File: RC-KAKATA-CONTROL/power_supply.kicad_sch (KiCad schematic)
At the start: 51 parts, among them J3 Screw_Terminal_01x02, J4 Screw_Terminal_01x02, U1 PS-TO220, U2 PS-TO220

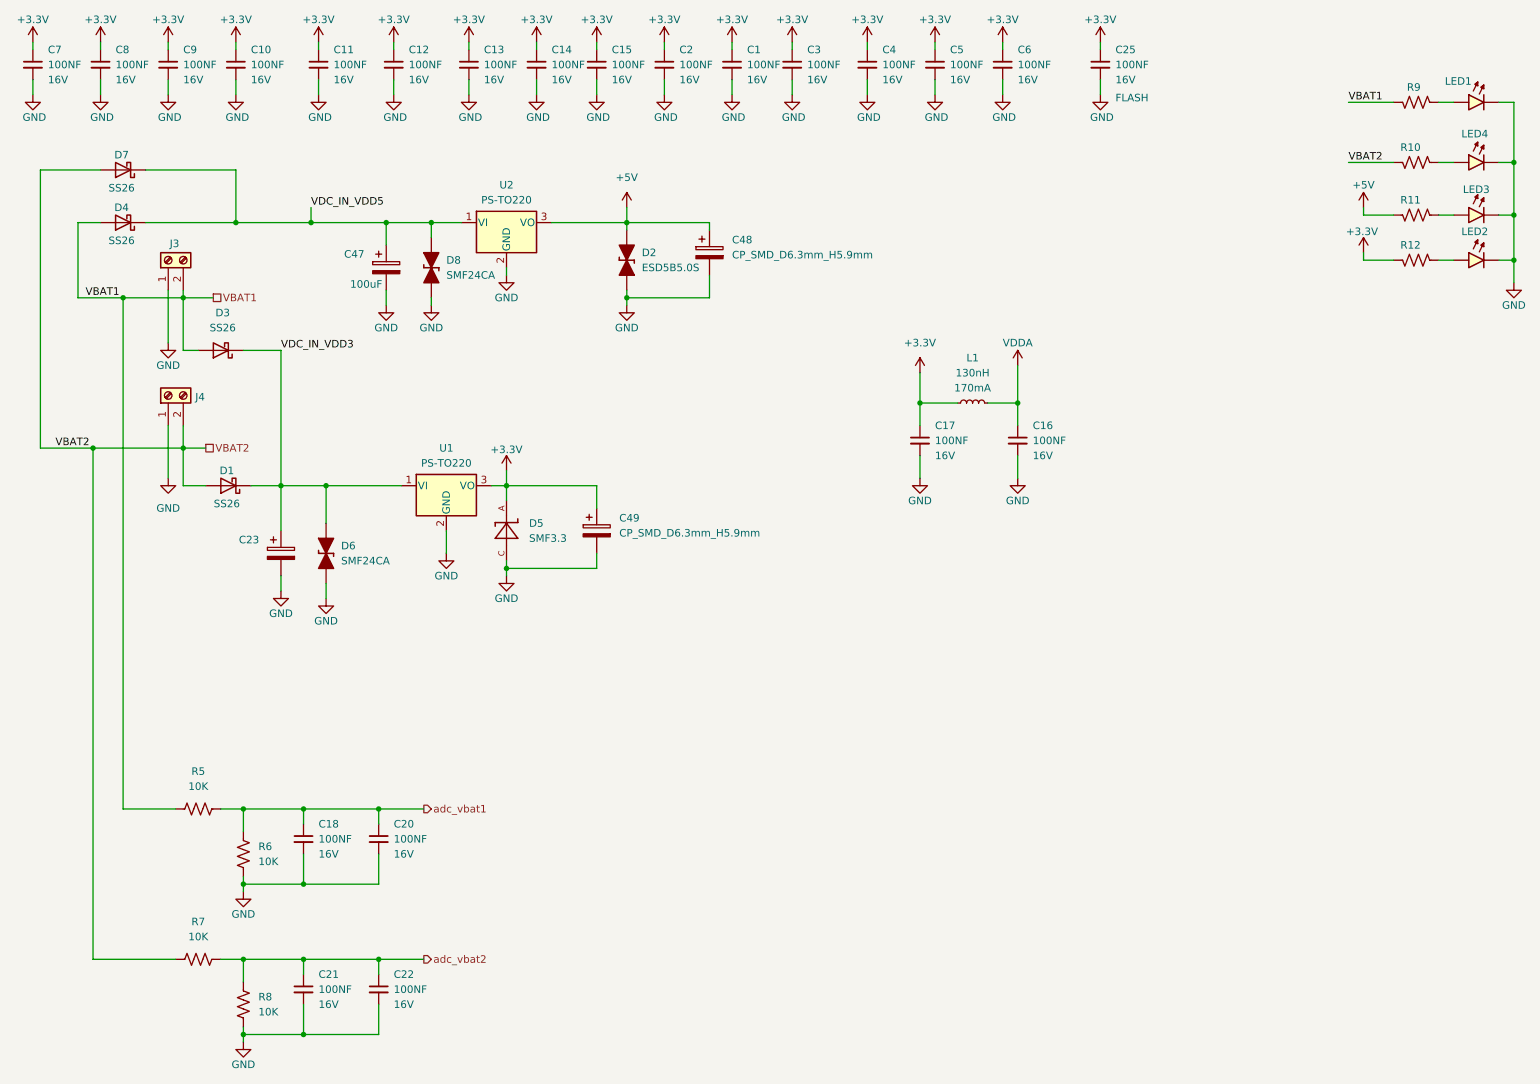
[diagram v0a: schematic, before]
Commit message: Agregadas conexiones de analogicos Agregadas las conexiones de i2c Agregadas las conexiones de Uart Cambiados algunos detalles de tvs resistencias y cap Recolocados los componenetes de power supply Cambiados los diodos de entrada de la bateria por unos de 5A Cambios menores y mejorada la documentacion Agregada informacion en la serigrafia del PCB
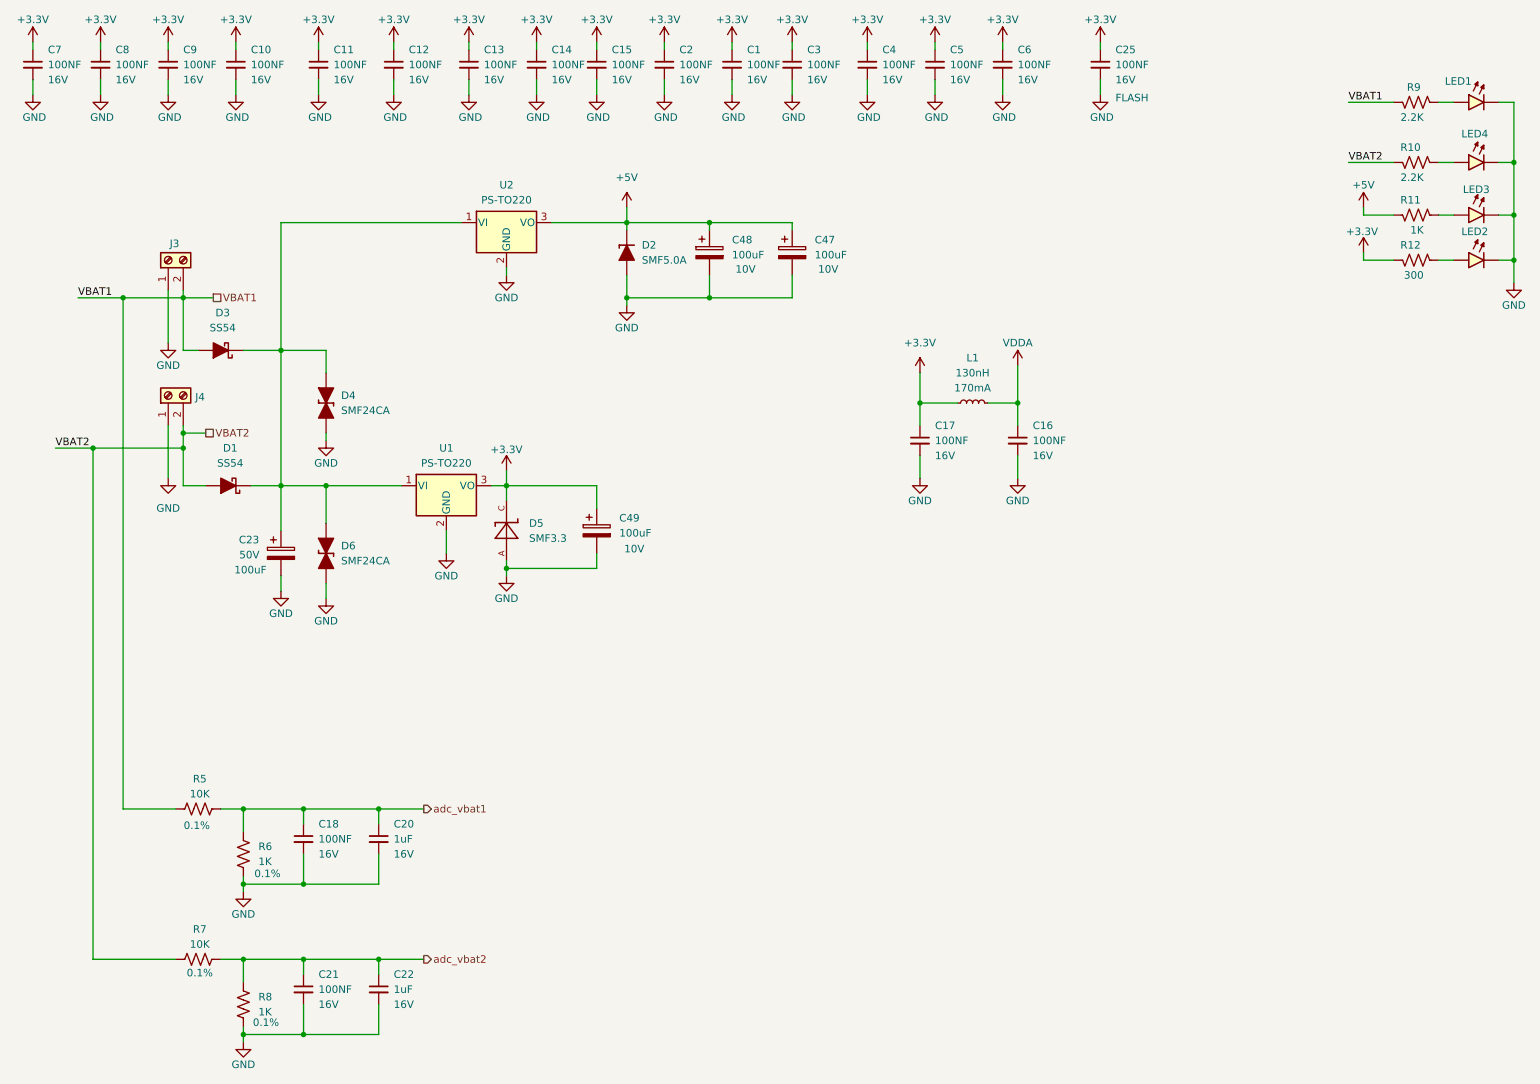
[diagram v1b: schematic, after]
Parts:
- removed C47: 100uF, Capacitor_SMD_AKL:CP_Elec_8x6.2, symbol Capacitor_AKL:CP_SMD_D8.0mm_H6.2mm
- removed D1, D3, D4, D7: SS26, Diode_SMD:D_SMA, symbol Diode:SS26
- removed D2: ESD5B5.0S, Diode_SMD_AKL:D_SOD-523, symbol Diode_TVS_AKL:ESD5B5.0S
- removed D8: SMF24CA, Diode_SMD_AKL:D_SOD-123F, symbol Diode_TVS_AKL:SMF24CA
- added C47: 100uF, Capacitor_SMD_AKL:CP_Elec_6.3x5.9, symbol Capacitor_AKL:CP_SMD_D6.3mm_H5.9mm
- added D1, D3: SS54, Diode_SMD_AKL:D_SMC, symbol Diode_Schottky_AKL:SS54
- added D2: SMF5.0A, Diode_SMD_AKL:D_SOD-123F, symbol Diode_TVS_AKL:SMF5.0A
- added D4: SMF24CA, Diode_SMD_AKL:D_SOD-123F, symbol Diode_TVS_AKL:SMF24CA
- C20, C22: value 100NF -> 1uF
- C23: value CP_SMD_D8.0mm_H6.2mm -> 100uF; VOL (none) -> 50V
- C48, C49: value CP_SMD_D6.3mm_H5.9mm -> 100uF; VOL (none) -> 10V
- R10, R9: value 10K -> 2.2K
- R11: value 10K -> 1K
- R12: value 10K -> 300
- R5, R7: VOL (none) -> 0.1%
- R6, R8: value 10K -> 1K; VOL (none) -> 0.1%
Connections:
- net VDC_IN_VDD5 is gone; now on an unnamed net: U2.1 (VI)
- net +3.3V: now also D5.C; no longer D5.A
- net +5V: now also C47.1, D2.1 (K)
- net GND: now also D5.A, C47.2, D2.2 (A), D4.1 (K); no longer D5.C
- net VBAT1: now also D3.2 (A)
- net VBAT2: now also D1.2 (A)
- net VDC_IN_VDD3: no longer names the net of C23.1, D6.2 (A), U1.1 (VI)
- net VDC_IN_VDD3: now also D1.1 (K), D3.1 (K), D4.2 (A)

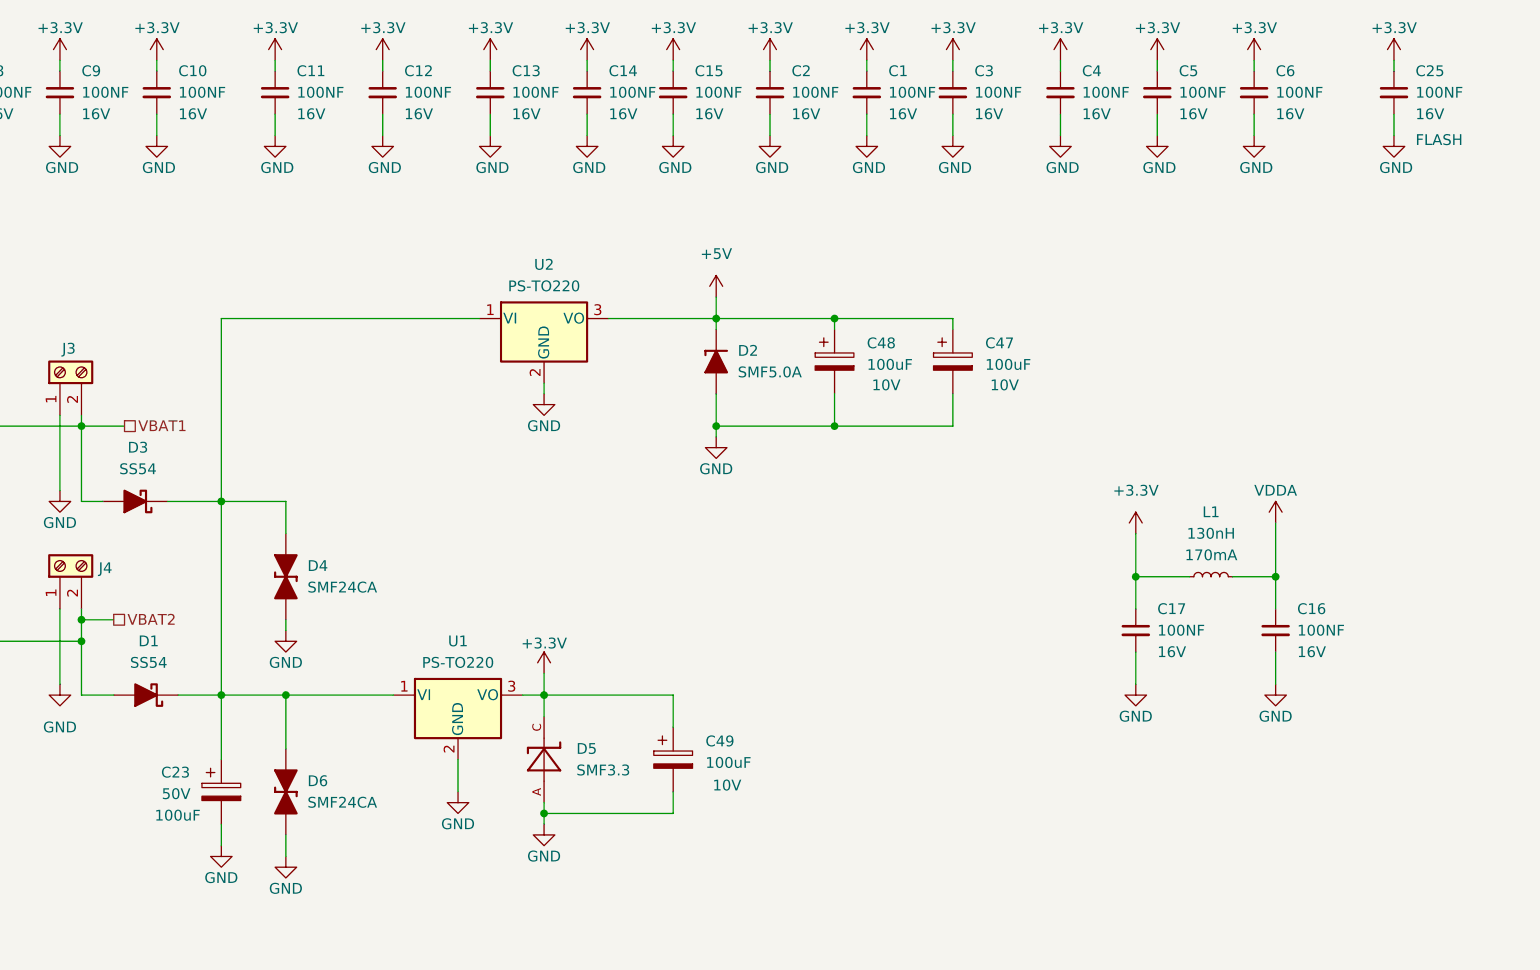
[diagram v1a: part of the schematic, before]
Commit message: Colocadas todas las piezas Verificacion de conexiones de los puertos UART - I2C - SPI Realizadas todas las conexiones Verificados los errores
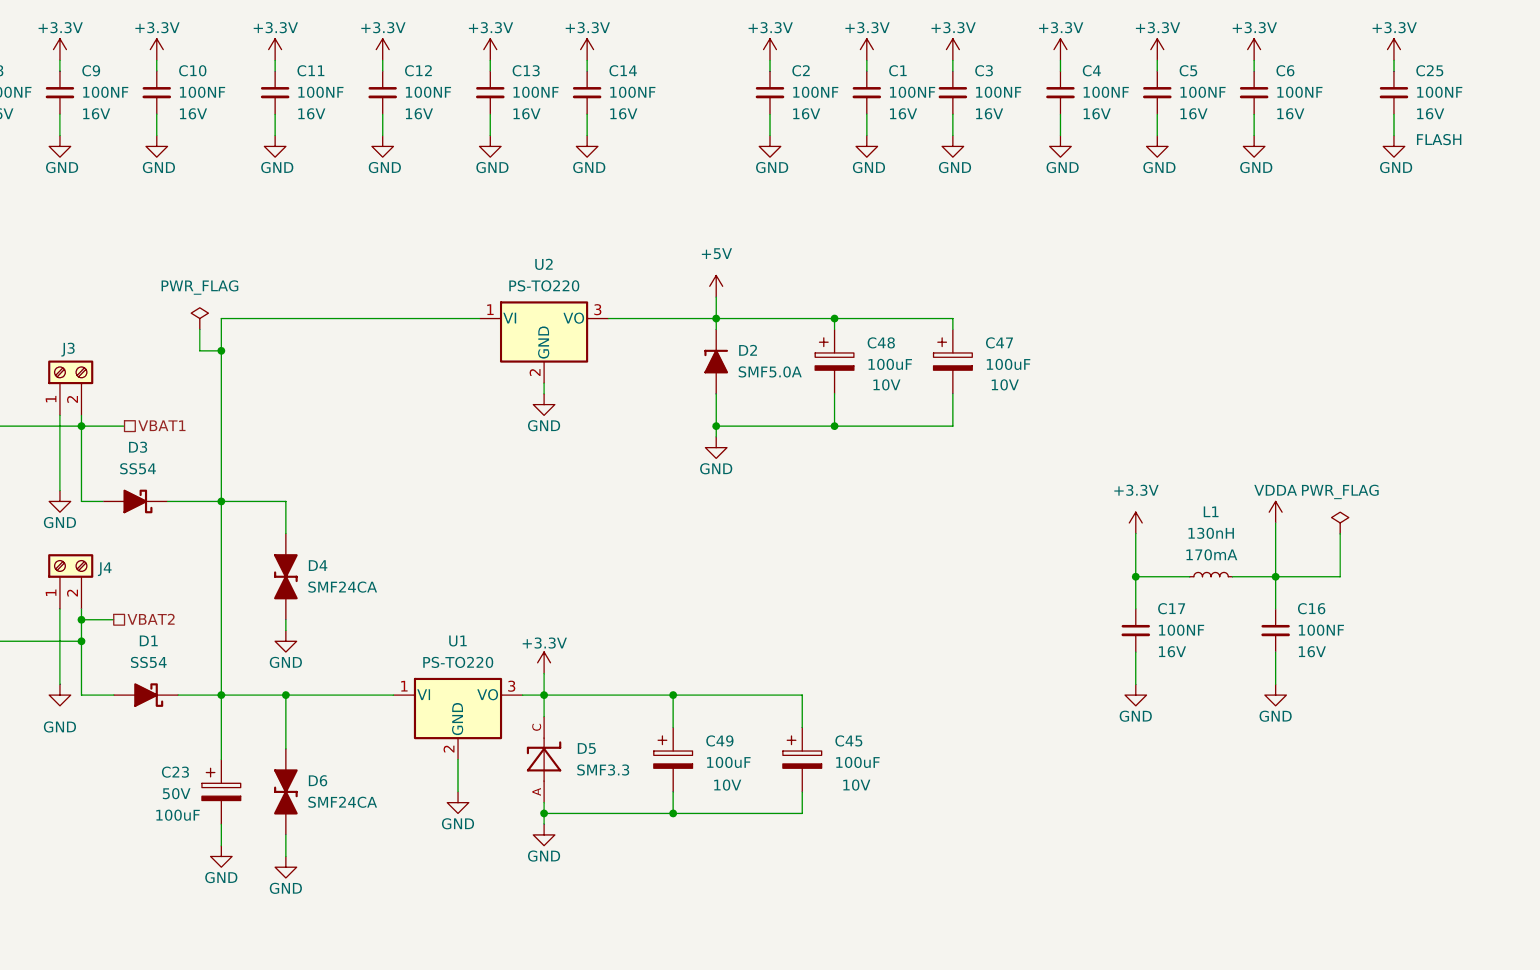
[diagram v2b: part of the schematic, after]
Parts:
- removed C15: 100NF, 4ms_Capacitor:C_0603, symbol MG_CAPACITOR:CAP-0603-100NF-16V-X5R
- added C45: 100uF, Capacitor_SMD_AKL:CP_Elec_6.3x5.9, symbol Capacitor_AKL:CP_SMD_D6.3mm_H5.9mm
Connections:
- net +3.3V: now also C45.1
- net GND: now also C45.2
